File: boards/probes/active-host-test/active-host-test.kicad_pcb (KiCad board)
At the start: 4 copper layers, 100 x 60 mm, 93 parts, among them J101 Conn_01x05_Male, J102 Barrel_Jack, J103 Conn_01x06_Male, J301 Conn_ARM_JTAG_SWD_10, J401 USB_C_Receptacle, Q401 Q_PNP_BEC, Q402 Q_NPN_BEC, Q403 Q_PMOS_GSD, Q404 Q_NMOS_GSD, U201 AP6502, U202 LM2611xMF, U203 AP2112K-3.3, U204 AP6502, U301 STM32F103V8Hx, U401 FUSB302BMPX, U402 STS232033B102, U403 STS232050B751, U404 STS232120B301, U405 LM66100, Y301 8MHz

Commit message: active-host-test: Fix issues with -7V supply
- Missing diode for Cuk converter
- Core needs to operate on 5V, not 12V
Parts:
- added C215: 0u1, Capacitor_SMD:C_0603_1608Metric, F.Cu at (59.8, 108.4)
- added D201: MBR0520, Diode_SMD:D_SOD-123, F.Cu at (68.6, 113.1)
- moved C202 4.47 mm to (60.5, 104.5), turned to 180 degrees
- moved C206 3.23 mm to (75.8, 112.1), turned to 270 degrees
- moved R205 2.98 mm to (72.0, 112.1), turned to 270 degrees
- moved R204 1.59 mm to (73.9, 112.1), turned to 270 degrees
- moved C205 1.02 mm to (64.2, 112.0)
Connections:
- U202 pad 4: /+12V -> +5V
- U202 pad 5: /+12V -> +5V
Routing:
- net Net-(C206-Pad2): track 13.0 -> 19.6 mm
- net +5V: track 64.2 -> 70.3 mm, vias 6 -> 8
- net /+12V: track 131.3 -> 126.1 mm
- net GND: track 132.5 -> 137.3 mm, vias 46 -> 49
- net Net-(C205-Pad1): track 4.18 -> 7.14 mm
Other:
- board text added: "STARSHIPRAIDER Active Probe Host Prototype RevB"
- board text removed: "STARSHIPRAIDER Active Probe Host Prototype RevA"

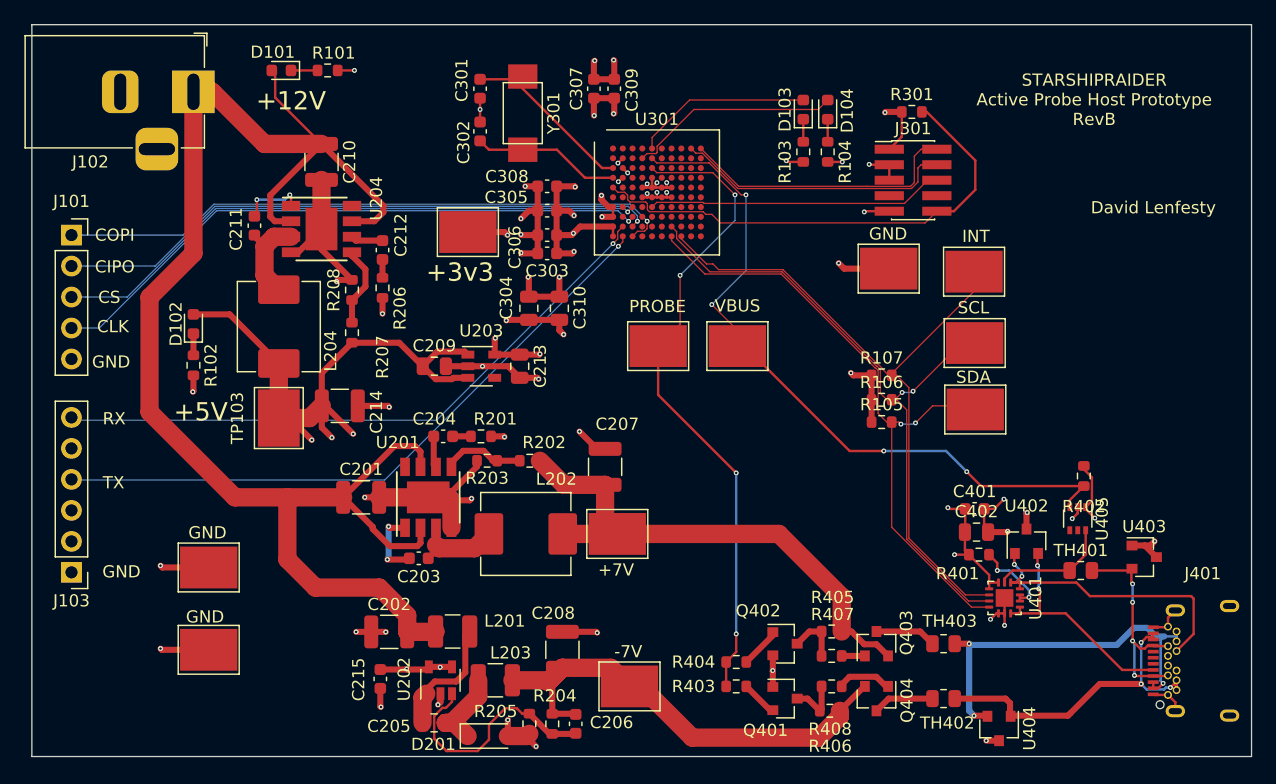
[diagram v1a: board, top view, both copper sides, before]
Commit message: probes/active-host-test: added errata and fixed some revA bugs
- replaced lm66100 w/ proper VBUS switch
- increased I2C pullup strength
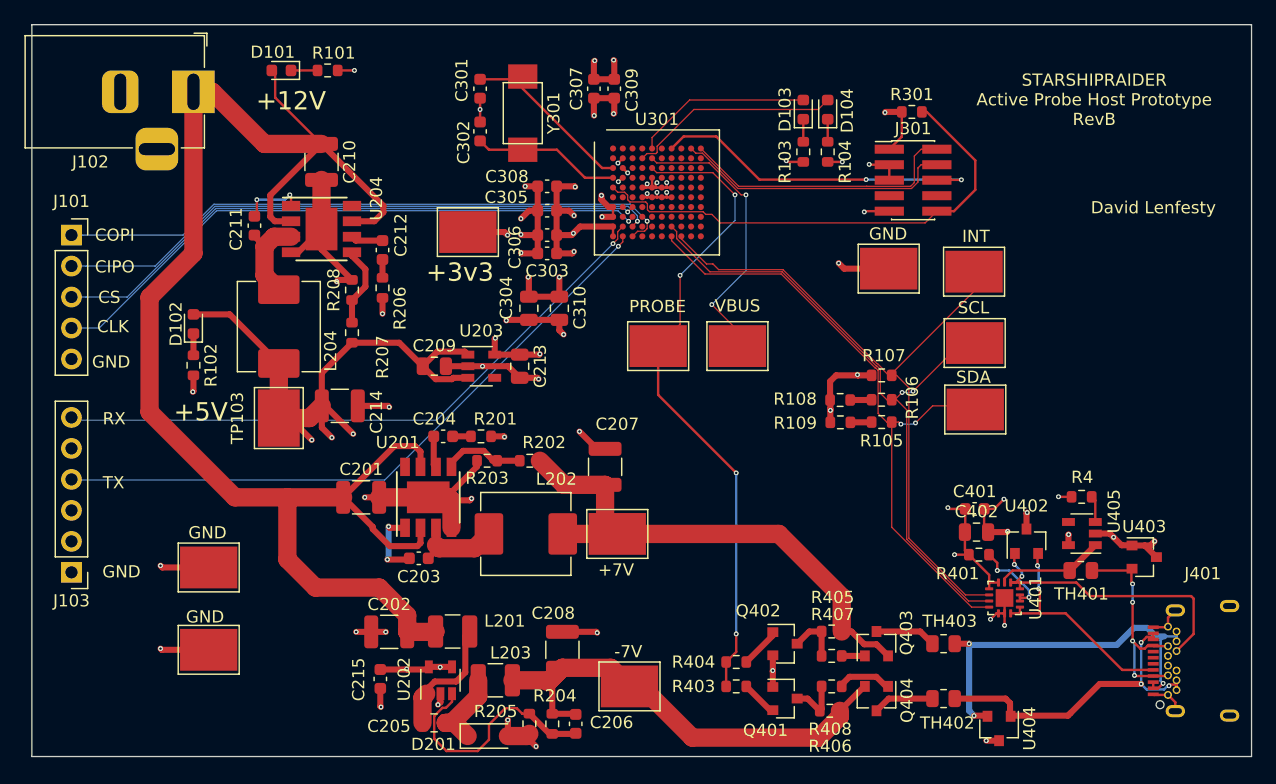
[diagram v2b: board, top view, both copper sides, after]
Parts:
- removed R402: 10k, Resistor_SMD:R_0603_1608Metric
- added R108: 1k, Resistor_SMD:R_0603_1608Metric, F.Cu at (97.5, 85.5)
- added R109: 1k, Resistor_SMD:R_0603_1608Metric, F.Cu at (97.5, 87.3)
- added R4: 10k, Resistor_SMD:R_0603_1608Metric, F.Cu at (117.3, 93.5)
- R105, R106: value 10k -> 1k
- U405: value LM66100 -> TPS2051C; footprint Package_TO_SOT_SMD:SOT-363_SC-70-6 -> Package_TO_SOT_SMD:SOT-23-5
- moved U405 1.27 mm to (117.3, 96.5), turned to 180 degrees
- turned R105 to 180 degrees
- turned R106 to 180 degrees
- turned R107 to 180 degrees
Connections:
- net Net-(U405-Pad4) renamed /USB C/VBUS_EN
- R105 pad 1: +3V3 -> /I2C_SDA
- R105 pad 2: /I2C_SDA -> Net-(R105-Pad2)
- R106 pad 1: +3V3 -> /I2C_SCL
- R106 pad 2: /I2C_SCL -> Net-(R106-Pad2)
- R107 pad 1: +3V3 -> /I2C_~INT
- R107 pad 2: /I2C_~INT -> +3V3
- U301 pad A7: Net-(U301-PadA7) -> /MCU/SWO
- U301 pad G5: /MCU/SWO -> Net-(U301-PadG5)
- U405 pad 1: +5V -> /USB C/VBUS
- U405 pad 3: /PROBE_VBUS_~EN -> Net-(R4-Pad1)
- U405 pad 5: Net-(U405-Pad5) -> +5V
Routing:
- net /PROBE_VBUS_~EN: track 58.7 -> 23.4 mm, vias 4 -> 2
- net /MCU/SWO: track 24.3 -> 27.7 mm, vias 0 -> 2
- net +5V: track 70.3 -> 67.2 mm, vias 8 -> 9
- net GND: track 137.3 -> 139.6 mm
- net Net-(R4-Pad1): track 0.00 -> 2.18 mm
- net Net-(R106-Pad2): track 0.00 -> 1.76 mm
- net Net-(R105-Pad2): track 0.00 -> 1.74 mm
- net +3V3: track 49.5 -> 51.0 mm, vias 18 -> 19
- net /USB C/VBUS: track 9.79 -> 8.91 mm
